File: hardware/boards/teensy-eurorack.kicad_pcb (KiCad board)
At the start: 2 copper layers, 64.8 x 109.2 mm, 52 parts, among them J1 Conn_01x03, J2 Conn_01x02, J27 Conn_01x02, J28 Conn_02x08_Odd_Even, J3 Conn_01x03, U2 AD5754BREZ, U3 AD5754BREZ, U4 Teensy4.1, U5 MCP1700-2502E, U6 AD7606BSTZ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

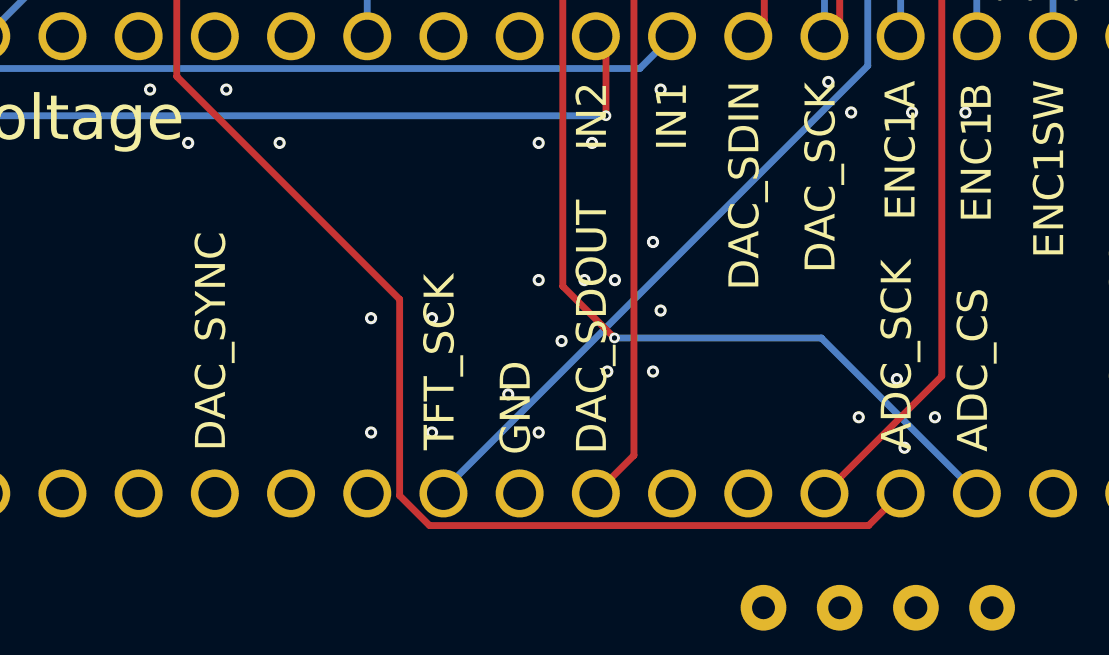
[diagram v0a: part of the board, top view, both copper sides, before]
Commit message: silkscreen corrections
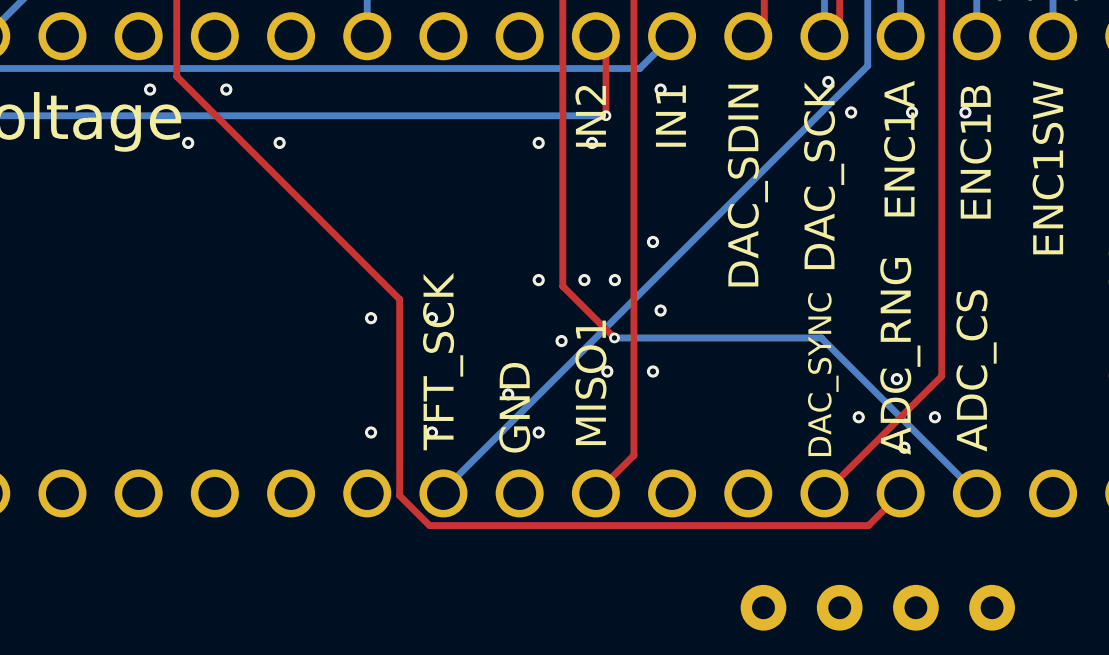
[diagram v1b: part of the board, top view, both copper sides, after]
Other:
- board text added: "ADC_RNG"
- board text added: "MISO1"
- board text removed: "ADC_SCK"
- board text removed: "DAC_SDOUT"
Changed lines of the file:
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@@
       (effects (font (size 1 1) (thickness 0.15)) (justify mirror))
     )
-    (pad "" smd roundrect (at 0.8 -1.67 180) (size 1.29 1.34) (layers B.Paste) (roundrect_rratio 0.193798))
-    (pad "" smd roundrect (at 0.8 0 180) (size 1.29 1.34) (layers B.Paste) (roundrect_rratio 0.193798))
-    (pad "" smd roundrect (at 0.8 1.67 180) (size 1.29 1.34) (layers B.Paste) (roundrect_rratio 0.193798))
-    (pad "" smd roundrect (at -0.8 -1.67 180) (size 1.29 1.34) (layers B.Paste) (roundrect_rratio 0.193798))
-    (pad "" smd roundrect (at -0.8 0 180) (size 1.29 1.34) (layers B.Paste) (roundrect_rratio 0.193798))
-    (pad "" smd roundrect (at -0.8 1.67 180) (size 1.29 1.34) (layers B.Paste) (roundrect_rratio 0.193798))
+    (pad "" smd roundrect (at 0.8 -1.67 180) (size 1.29 1.34) (layers B.Paste) (roundrect_rratio 0.1937976744186047))
+    (pad "" smd roundrect (at 0.8 0 180) (size 1.29 1.34) (layers B.Paste) (roundrect_rratio 0.1937976744186047))
+    (pad "" smd roundrect (at 0.8 1.67 180) (size 1.29 1.34) (layers B.Paste) (roundrect_rratio 0.1937976744186047))
+    (pad "" smd roundrect (at -0.8 -1.67 180) (size 1.29 1.34) (layers B.Paste) (roundrect_rratio 0.1937976744186047))
+    (pad "" smd roundrect (at -0.8 0 180) (size 1.29 1.34) (layers B.Paste) (roundrect_rratio 0.1937976744186047))
+    (pad "" smd roundrect (at -0.8 1.67 180) (size 1.29 1.34) (layers B.Paste) (roundrect_rratio 0.1937976744186047))
     (pad 25 smd rect (at 0 0 180) (size 3.2 5) (layers B.Cu B.Mask)
       (net 5 -12V))
@@
       (effects (font (size 1 1) (thickness 0.15)) (justify mirror))
     )
-    (pad "" smd roundrect (at 0.8 -1.67 180) (size 1.29 1.34) (layers B.Paste) (roundrect_rratio 0.193798))
-    (pad "" smd roundrect (at 0.8 0 180) (size 1.29 1.34) (layers B.Paste) (roundrect_rratio 0.193798))
-    (pad "" smd roundrect (at 0.8 1.67 180) (size 1.29 1.34) (layers B.Paste) (roundrect_rratio 0.193798))
-    (pad "" smd roundrect (at -0.8 -1.67 180) (size 1.29 1.34) (layers B.Paste) (roundrect_rratio 0.193798))
-    (pad "" smd roundrect (at -0.8 0 180) (size 1.29 1.34) (layers B.Paste) (roundrect_rratio 0.193798))
-    (pad "" smd roundrect (at -0.8 1.67 180) (size 1.29 1.34) (layers B.Paste) (roundrect_rratio 0.193798))
+    (pad "" smd roundrect (at 0.8 -1.67 180) (size 1.29 1.34) (layers B.Paste) (roundrect_rratio 0.1937976744186047))
+    (pad "" smd roundrect (at 0.8 0 180) (size 1.29 1.34) (layers B.Paste) (roundrect_rratio 0.1937976744186047))
+    (pad "" smd roundrect (at 0.8 1.67 180) (size 1.29 1.34) (layers B.Paste) (roundrect_rratio 0.1937976744186047))
+    (pad "" smd roundrect (at -0.8 -1.67 180) (size 1.29 1.34) (layers B.Paste) (roundrect_rratio 0.1937976744186047))
+    (pad "" smd roundrect (at -0.8 0 180) (size 1.29 1.34) (layers B.Paste) (roundrect_rratio 0.1937976744186047))
+    (pad "" smd roundrect (at -0.8 1.67 180) (size 1.29 1.34) (layers B.Paste) (roundrect_rratio 0.1937976744186047))
     (pad 25 smd rect (at 0 0 180) (size 3.2 5) (layers B.Cu B.Mask)
       (net 5 -12V))
@@
       (net 4 +5V))
   )
+  (gr_text DAC_SYNC (at 156.21 133.731 90) (layer F.SilkS)
+    (effects (font (size 0.762 0.762) (thickness 0.127)))
+  )
   (gr_text VIN8 (at 168.492667 64.77) (layer F.SilkS)
     (effects (font (size 1 1) (thickness 0.15)) (justify right))
@@
     (effects (font (size 1 1) (thickness 0.15)))
   )
-  (gr_text ADC_SCK (at 158.75 133.048333 90) (layer F.SilkS)
+  (gr_text ADC_RNG (at 158.75 133.048333 90) (layer F.SilkS)
     (effects (font (size 1 1) (thickness 0.15)))
   )
@@
     (effects (font (size 1 1) (thickness 0.15)))
   )
-  (gr_text DAC_SDOUT (at 148.59 132.119762 90) (layer F.SilkS)
+  (gr_text MISO1 (at 148.59 133.985 90) (layer F.SilkS)
     (effects (font (size 1 1) (thickness 0.15)))
   )
@@
     (effects (font (size 1 1) (thickness 0.15)))
   )
-  (gr_text DAC_SYNC (at 135.89 132.595952 90) (layer F.SilkS)
-    (effects (font (size 1 1) (thickness 0.15)))
-  )

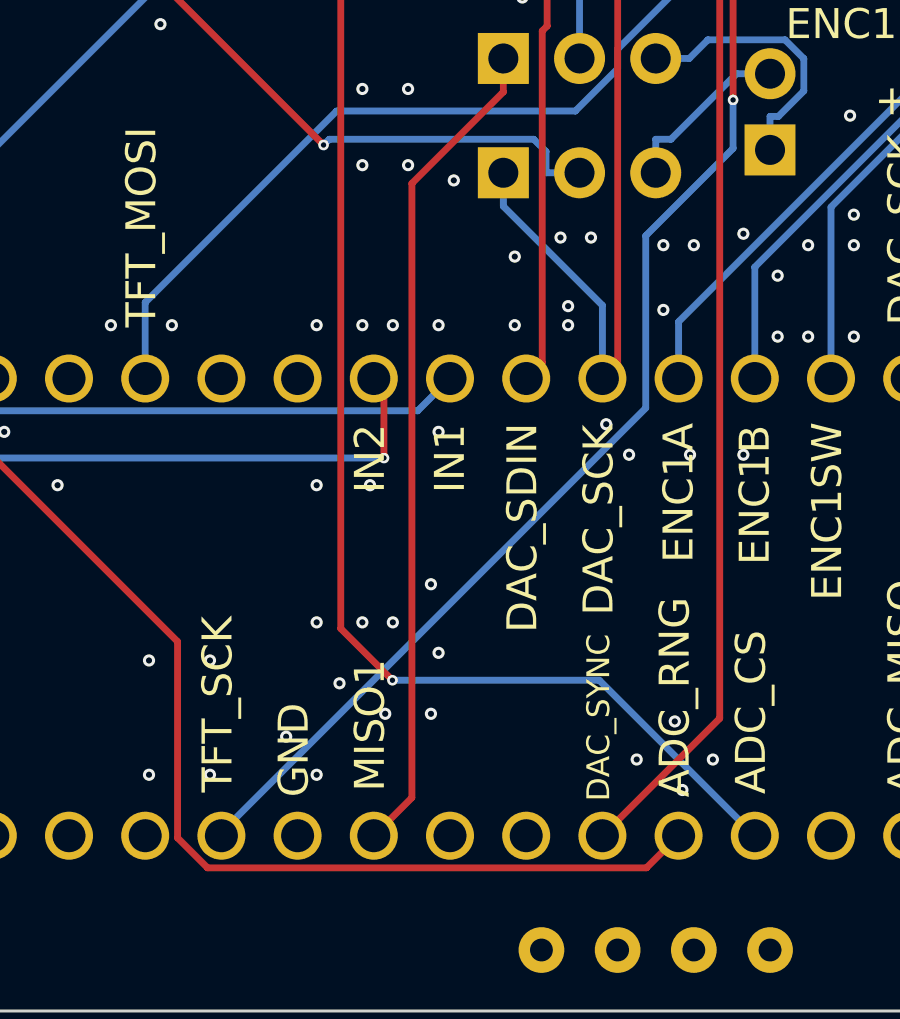
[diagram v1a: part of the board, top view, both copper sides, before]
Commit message: corrections applied to pcb, miso to pin 39
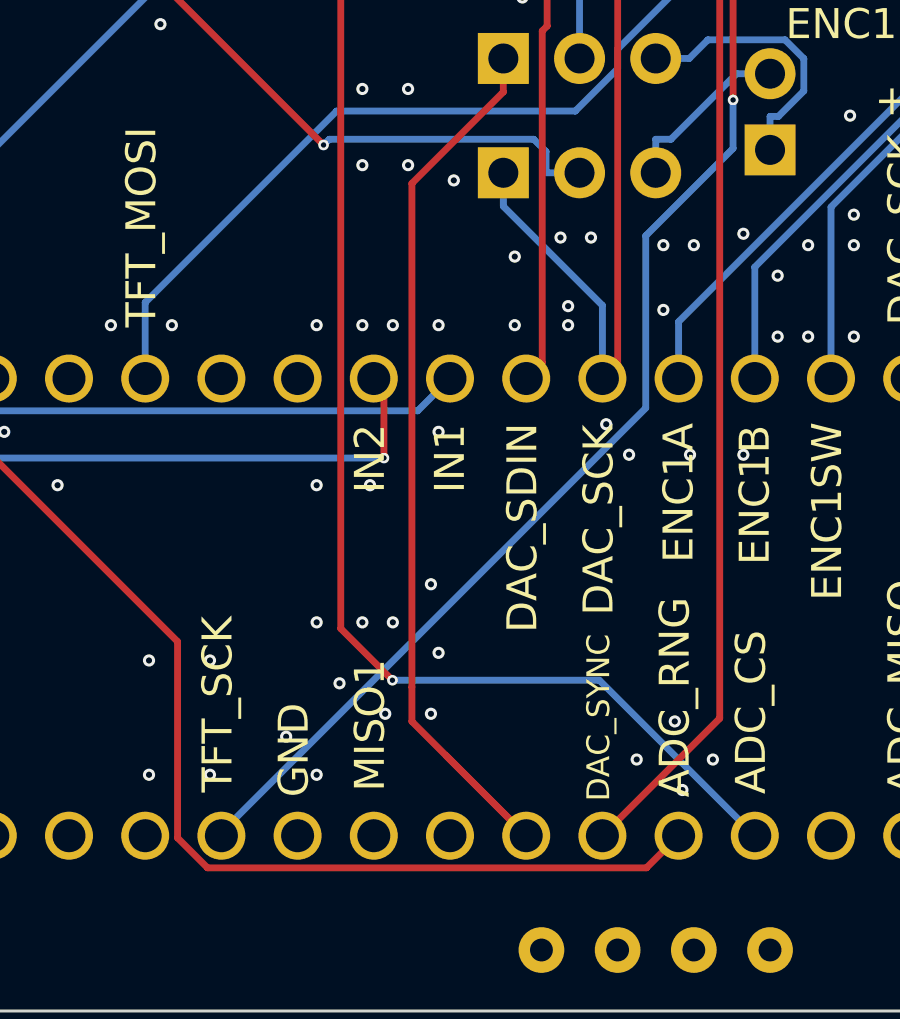
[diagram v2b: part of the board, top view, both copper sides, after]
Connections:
- BB1 pad 20: (no net) -> Net-(BB1-Pad20)
- BB1 pad 41: (no net) -> Net-(BB1-Pad41)
- BB1 pad 42: (no net) -> Net-(BB1-Pad42)
- BB1 pad 43: (no net) -> Net-(BB1-Pad43)
- BB1 pad 53: (no net) -> Net-(BB1-Pad53)
- BB1 pad 54: (no net) -> Net-(BB1-Pad54)
- BB1 pad 55: (no net) -> Net-(BB1-Pad55)
- BB1 pad 56: (no net) -> Net-(BB1-Pad56)
- J28 pad 13: (no net) -> Net-(J28-Pad13)
- J28 pad 14: (no net) -> Net-(J28-Pad14)
- J28 pad 15: (no net) -> Net-(J28-Pad15)
- J28 pad 16: (no net) -> Net-(J28-Pad16)
- U2 pad 12: (no net) -> Net-(U2-Pad12)
- U2 pad 13: (no net) -> Net-(U2-Pad13)
- U2 pad 2: (no net) -> Net-(U2-Pad2)
- U2 pad 6: (no net) -> Net-(U2-Pad6)
- U3 pad 12: (no net) -> Net-(U3-Pad12)
- U3 pad 13: (no net) -> Net-(U3-Pad13)
- U3 pad 16: (no net) -> Net-(U3-Pad16)
- U3 pad 2: (no net) -> Net-(U3-Pad2)
- U3 pad 6: (no net) -> Net-(U3-Pad6)
- U4 pad 10: (no net) -> Net-(U4-Pad10)
- U4 pad 11: (no net) -> Net-(U4-Pad11)
- U4 pad 12: (no net) -> Net-(U4-Pad12)
- U4 pad 14: (no net) -> Net-(U4-Pad14)
- U4 pad 15: (no net) -> Net-(U4-Pad15)
- U4 pad 23: (no net) -> Net-(U4-Pad23)
- U4 pad 24: (no net) -> Net-(U4-Pad24)
- U4 pad 25: (no net) -> Net-(U4-Pad25)
- U4 pad 26: (no net) -> Net-(U4-Pad26)
- U4 pad 27: (no net) -> Net-(U4-Pad27)
- U4 pad 31: (no net) -> /MISO1
- U4 pad 32: (no net) -> Net-(U4-Pad32)
- U4 pad 33: /MISO1 -> Net-(U4-Pad33)
- U4 pad 36: (no net) -> Net-(U4-Pad36)
- U4 pad 37: (no net) -> Net-(U4-Pad37)
- U4 pad 38: (no net) -> Net-(U4-Pad38)
- U4 pad 39: (no net) -> Net-(U4-Pad39)
- U4 pad 40: (no net) -> Net-(U4-Pad40)
- U4 pad 41: (no net) -> Net-(U4-Pad41)
- U4 pad 42: (no net) -> Net-(U4-Pad42)
- U4 pad 43: (no net) -> Net-(U4-Pad43)
- U4 pad 44: (no net) -> Net-(U4-Pad44)
- U4 pad 45: (no net) -> Net-(U4-Pad45)
- U4 pad 9: (no net) -> Net-(U4-Pad9)
- U6 pad 15: (no net) -> Net-(U6-Pad15)
- U6 pad 42: (no net) -> Net-(U6-Pad42)
- U7 pad 1: (no net) -> Net-(U7-Pad1)
- U7 pad 4: (no net) -> Net-(U7-Pad4)
- U7 pad 7: (no net) -> Net-(U7-Pad7)
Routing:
- net /MISO1: track 27.7 -> 32.5 mm

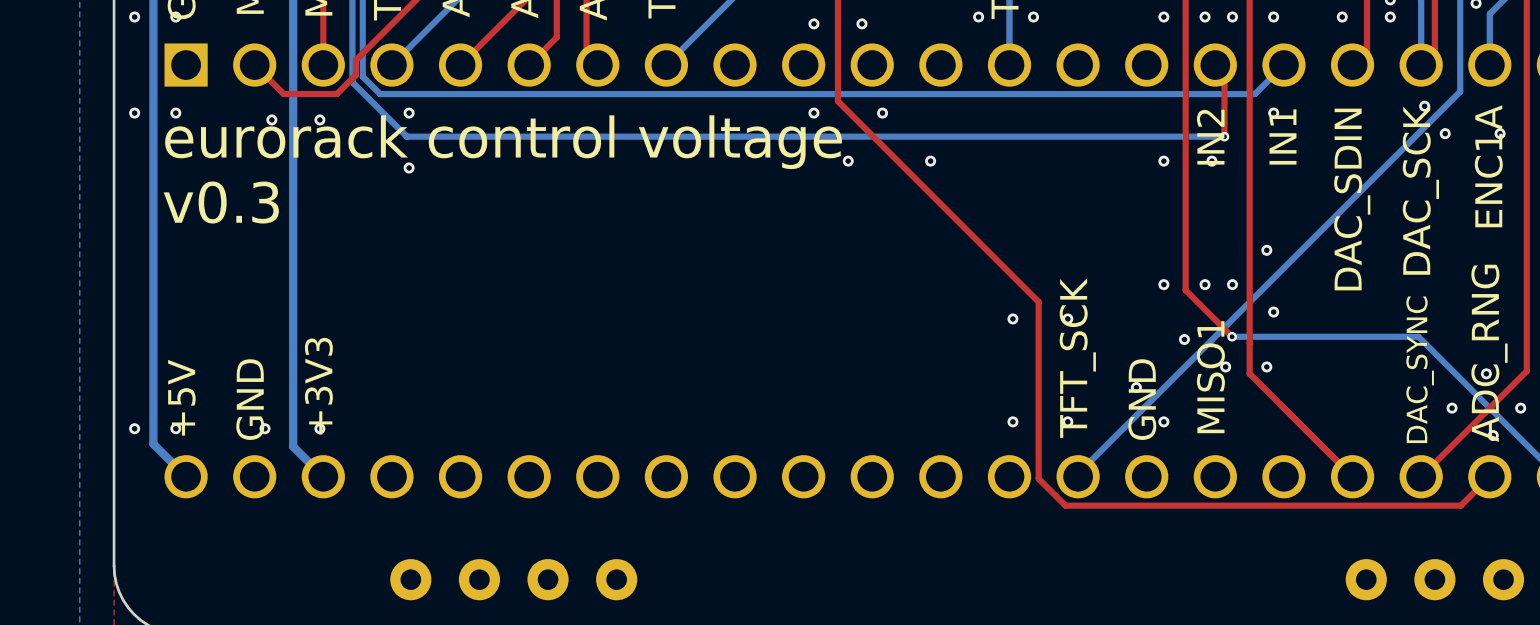
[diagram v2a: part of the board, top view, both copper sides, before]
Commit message: silkscreen corrections and updated to version 0.4
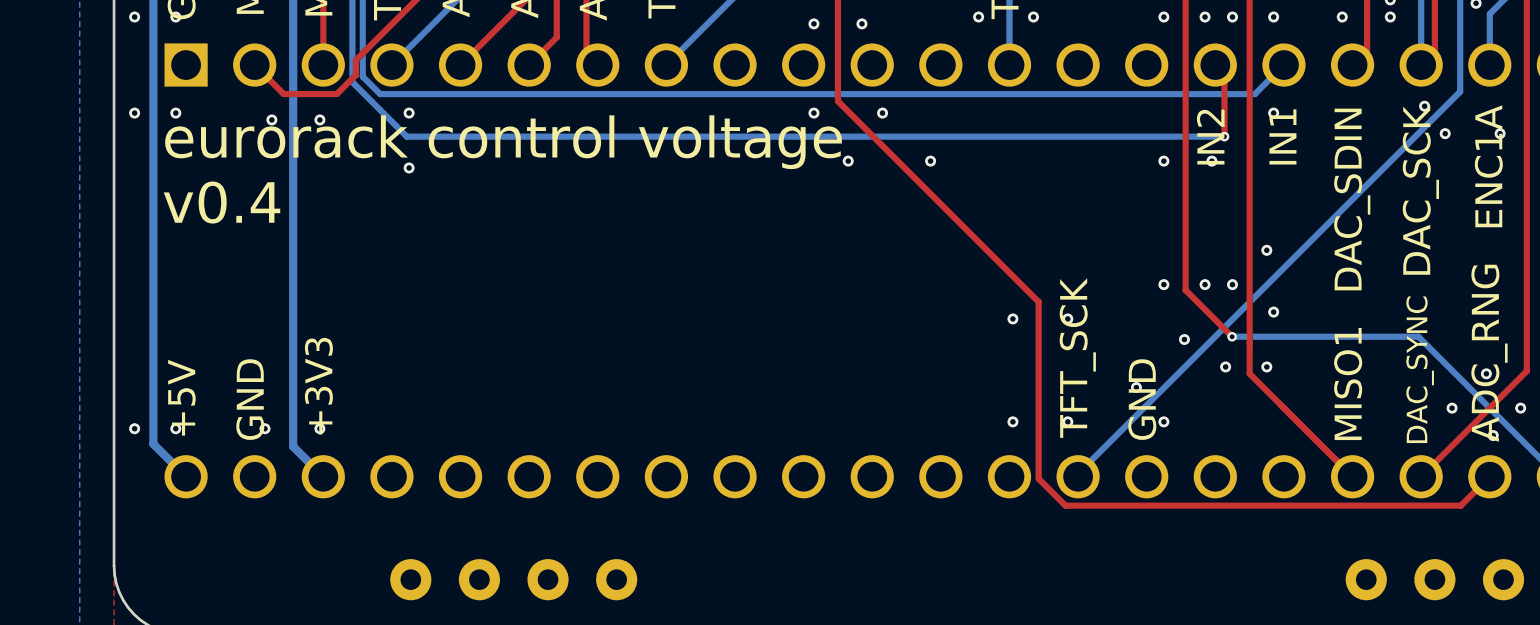
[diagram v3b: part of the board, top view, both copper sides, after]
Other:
- board text added: "eurorack control voltage v0.4"
- board text added: "https://github.com/newdigate/teensy-control-voltage version 0.4"
- board text removed: "eurorack control voltage v0.3"
- board text removed: "https://github.com/newdigate/teensy-control-voltage version 0.3"
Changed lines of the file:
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@@
     (effects (font (size 1 1) (thickness 0.15)))
   )
-  (gr_text MISO1 (at 148.59 133.985 90) (layer F.SilkS)
+  (gr_text MISO1 (at 153.67 134.239 90) (layer F.SilkS)
     (effects (font (size 1 1) (thickness 0.15)))
   )
@@
     (effects (font (size 0.762 0.762) (thickness 0.127)) (justify right mirror))
   )
-  (gr_text "https://github.com/newdigate/teensy-control-voltage\nversion 0.3" (at 169.545 40.64) (layer B.SilkS)
+  (gr_text "https://github.com/newdigate/teensy-control-voltage\nversion 0.4" (at 169.545 40.64) (layer B.SilkS)
     (effects (font (size 1 1) (thickness 0.15)) (justify left mirror))
   )
-  (gr_text "eurorack control voltage\nv0.3" (at 109.728 126.365) (layer F.SilkS)
+  (gr_text "eurorack control voltage\nv0.4" (at 109.728 126.365) (layer F.SilkS)
     (effects (font (size 1.5 1.5) (thickness 0.3)) (justify left))
   )
